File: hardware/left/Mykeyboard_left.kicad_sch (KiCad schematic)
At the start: 80 parts, among them J1 OLED_128x32, U1 RP2040_Zero

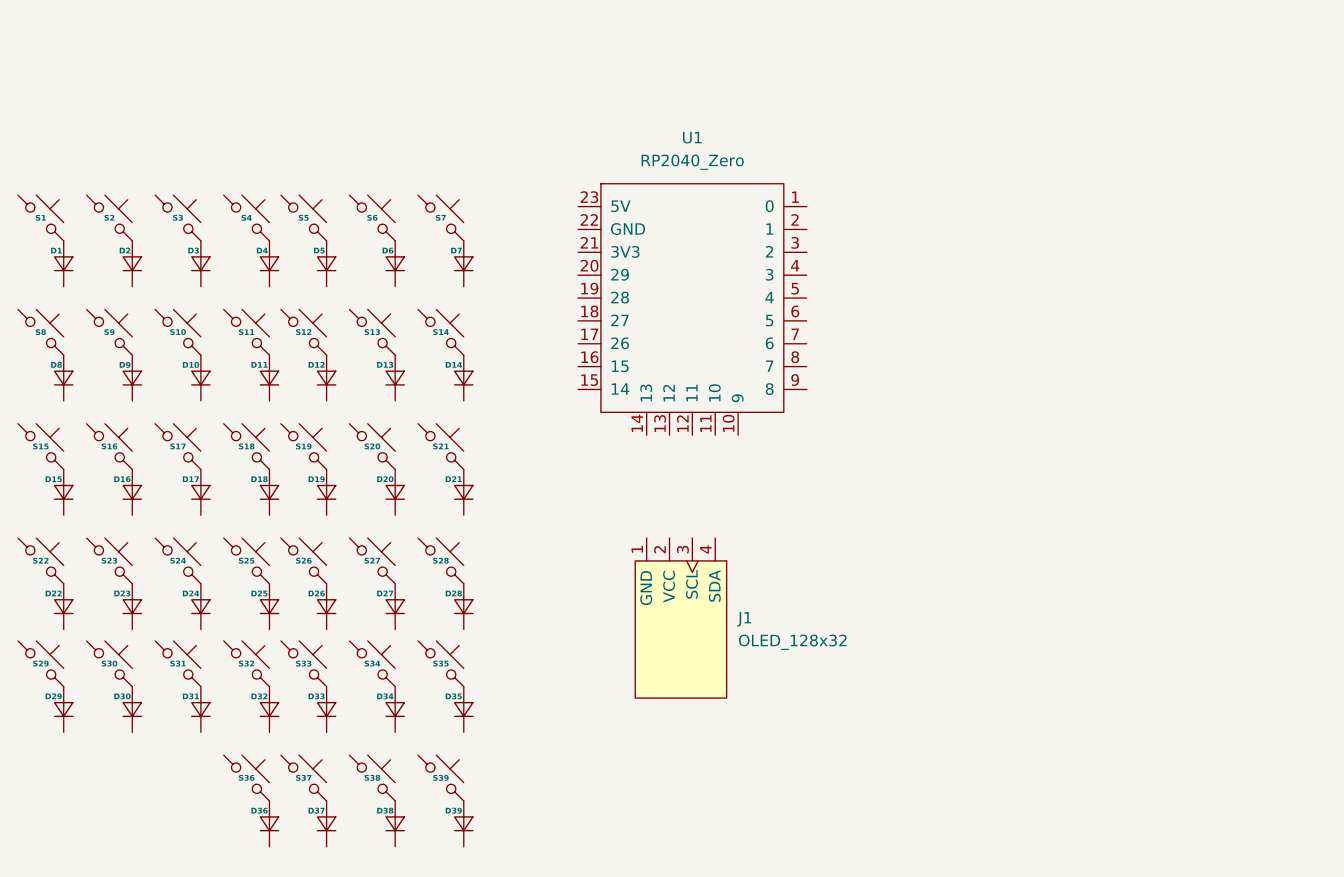
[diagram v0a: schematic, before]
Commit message: Divide hardware en mitades left/right, mueve framework QMK a firmware/, añade docs
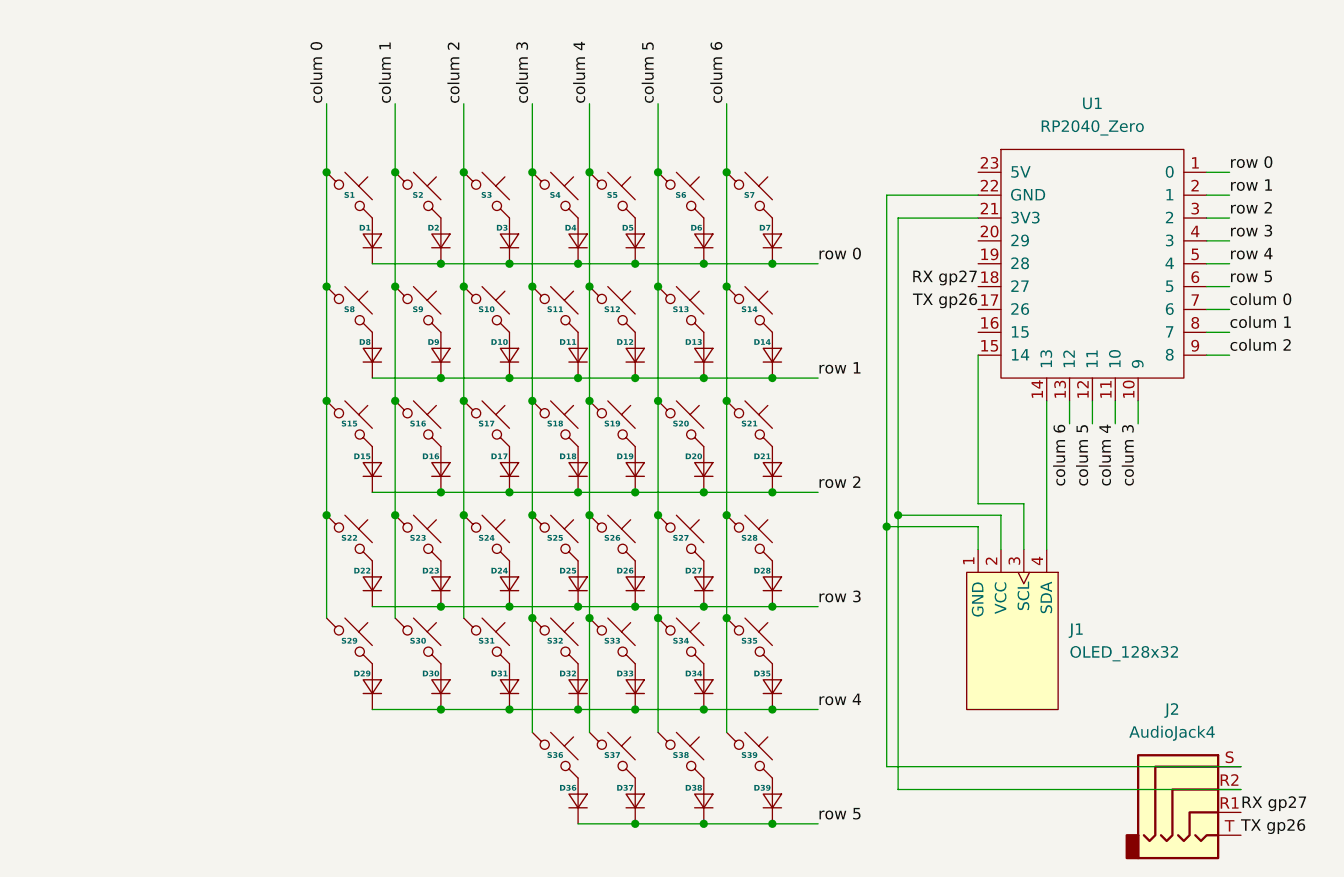
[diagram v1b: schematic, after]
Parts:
- added J2: AudioJack4, Connector_Audio:Jack_3.5mm_PJ320D_Horizontal, symbol Connector_Audio:AudioJack4
- D1, D10, D11, D12, D13, D14, D15, D16, D17, D18, D19, D2, D20, D21, D22, D23, D24, D25, D26, D27, D28, D29, D3, D30, D31, D32, D33, D34, D35, D36, D37, D38, D39, D4, D5, D6, D7, D8, D9: footprint ScottoKeebs_Components:Encoder_Ano -> ScottoKeebs_Components:Diode_DO-35
- S1, S10, S11, S12, S13, S14, S15, S16, S17, S18, S19, S2, S20, S21, S22, S23, S24, S25, S26, S27, S28, S29, S3, S30, S31, S32, S33, S34, S35, S36, S37, S38, S39, S4, S5, S6, S7, S8, S9: footprint (none) -> ScottoKeebs_MX:MX_PCB_1.00u
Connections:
- net row 2: now reaches D16.1 (K)
- net row 2: now also D15.1 (K), D17.1 (K), D18.1 (K), D19.1 (K), D20.1 (K), D21.1 (K), U1.3 (2)
- net colum 6: now reaches S14.1
- net colum 6: now also S21.1, S28.1, S35.1, S39.1, S7.1, U1.13 (12)
- net colum 3: now reaches S25.1
- net colum 3: now also S11.1, S18.1, S32.1, S36.1, S4.1, U1.10 (9)
- net row 5: now reaches D38.1 (K)
- net row 5: now also D36.1 (K), D37.1 (K), D39.1 (K), U1.6 (5)
- net colum 4: now reaches S26.1
- net colum 4: now also S12.1, S19.1, S33.1, S37.1, S5.1, U1.11 (10)
- net colum 1: now reaches S9.1
- net colum 1: now also S16.1, S2.1, S23.1, S30.1, U1.8 (7)
- net colum 0: now reaches S1.1
- net colum 0: now also S15.1, S22.1, S29.1, S8.1, U1.7 (6)
- net row 4: now reaches D30.1 (K)
- net row 4: now also D29.1 (K), D31.1 (K), D32.1 (K), D33.1 (K), D34.1 (K), D35.1 (K), U1.5 (4)
- net row 1: now reaches D8.1 (K)
- net row 1: now also D10.1 (K), D11.1 (K), D12.1 (K), D13.1 (K), D14.1 (K), D9.1 (K), U1.2 (1)
- net colum 2: now reaches S10.1
- net colum 2: now also S17.1, S24.1, S3.1, S31.1, U1.9 (8)
- net row 3: now reaches D23.1 (K)
- net row 3: now also D22.1 (K), D24.1 (K), D25.1 (K), D26.1 (K), D27.1 (K), D28.1 (K), U1.4 (3)
- net colum 5: now reaches S13.1
- net colum 5: now also S20.1, S27.1, S34.1, S38.1, S6.1, U1.12 (11)
- net row 0: now reaches D6.1 (K)
- net row 0: now also D1.1 (K), D2.1 (K), D3.1 (K), D4.1 (K), D5.1 (K), D7.1 (K), U1.1 (0)
- net at J1.1 (GND): now also U1.22 (GND), J2.S
- net at J1.2 (VCC): now also U1.21 (3V3), J2.R2
- net at J1.3 (SCL): now also U1.15 (14)
- net at J1.4 (SDA): now also U1.14 (13)
- net TX gp26: now reaches U1.17 (26)
- net TX gp26: now also J2.T
- net RX gp27: now reaches U1.18 (27)
- net RX gp27: now also J2.R1
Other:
- moved on the sheet: D1, D10, D11, D12, D13, D14, D15, D16, D17, D18, D19, D2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
